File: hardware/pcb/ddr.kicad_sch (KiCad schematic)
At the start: 30 parts, among them U2 MT41K256M16TW

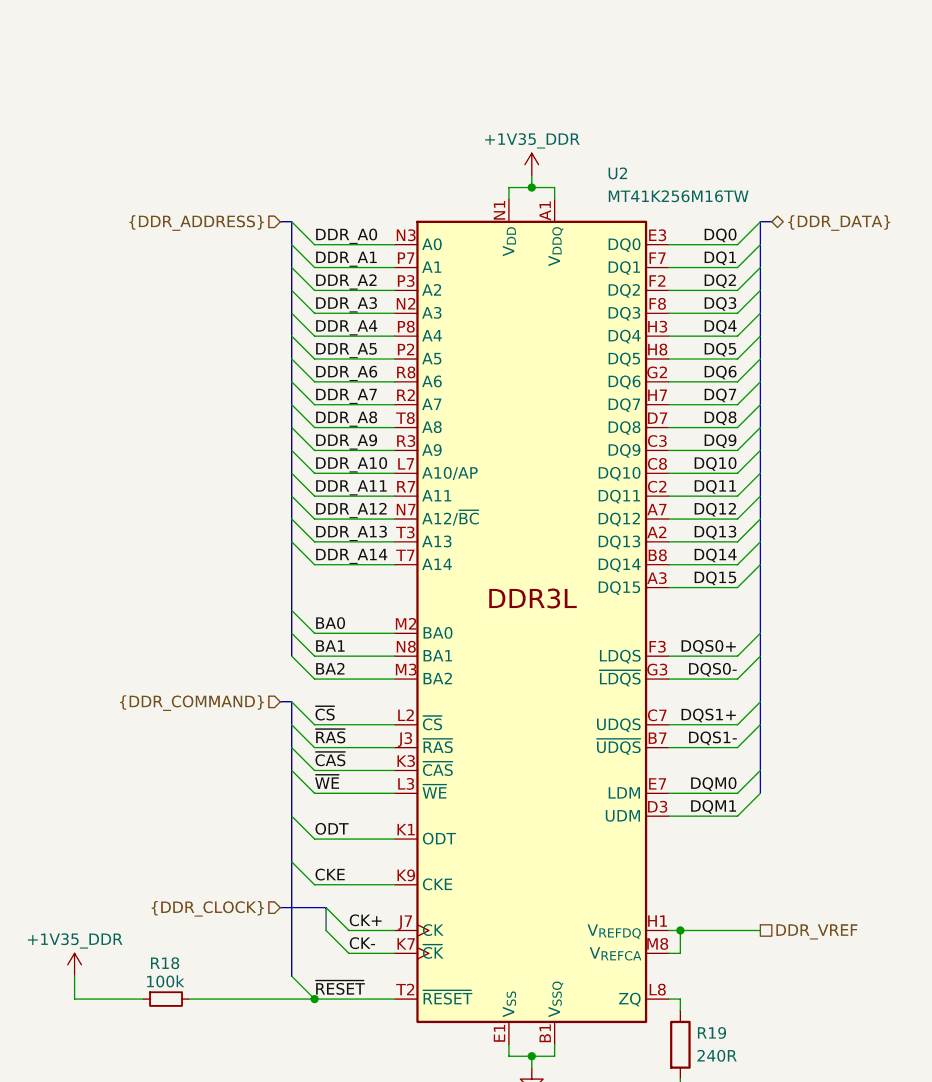
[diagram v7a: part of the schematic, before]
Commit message: changed stackup, creted tuning profiles, created net classes
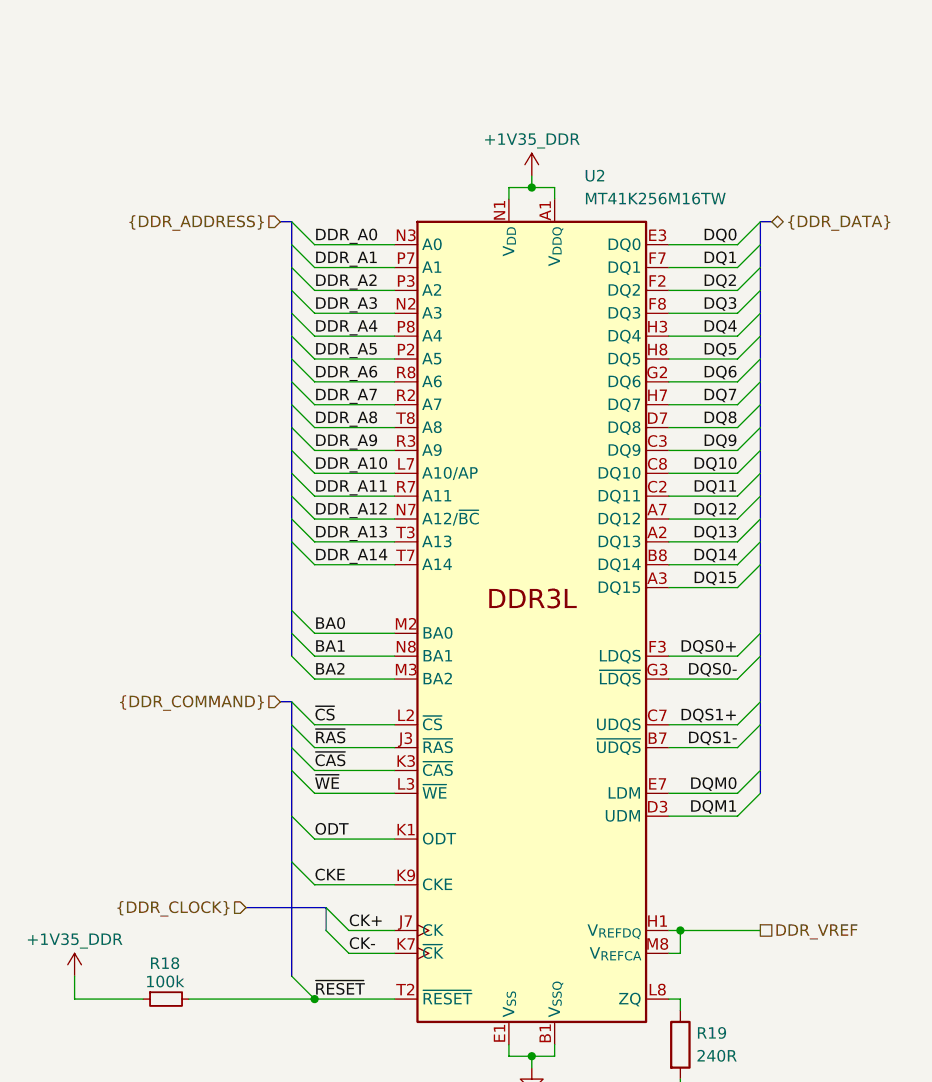
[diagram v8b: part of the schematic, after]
